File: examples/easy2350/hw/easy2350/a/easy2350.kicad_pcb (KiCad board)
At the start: 4 copper layers, 21 x 51 mm, 58 parts, among them J1 USB-C, J2 GPIO left, J3 GPIO right, J4 SWD, SW1 BOOTSEL, SW2 RESET, U1 RP2350A, U2 USBLC6-2SC6, U3 AP7361C-33FGE, U4 SN74LV1T125DBVR, U5 W25Q128JVSIQ, Y1 12MHz

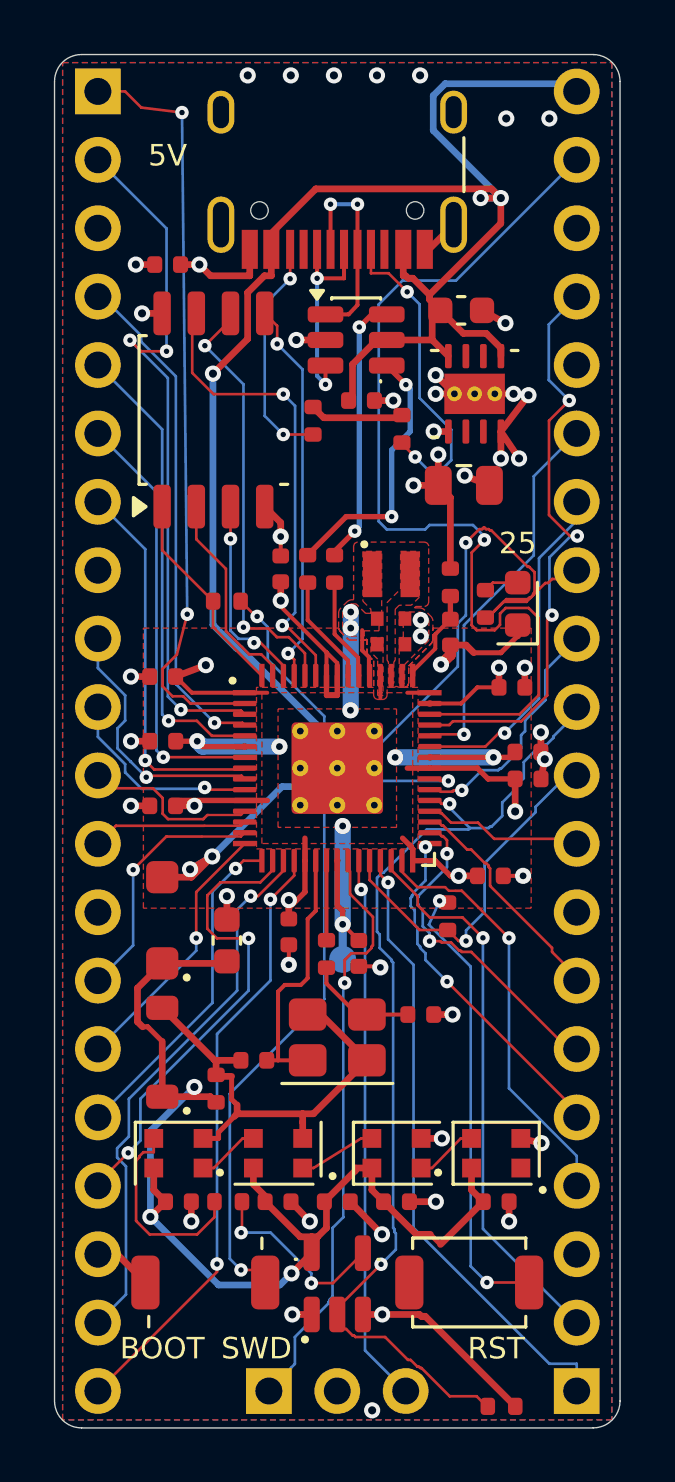
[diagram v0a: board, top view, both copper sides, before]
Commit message: easy2350: re-routed with ultraroute from a bare board, no locked copper
The user: easy2350 should not be locked like that; it should route
deterministically with ultraroute. Every locked track and via is gone (the
vendor regulator copy, the critical pre-routes, the pad vias, the band stubs
and VBUS twins: 232 items) and the router lays the whole board. Footprints are
locked only where Circuit Composer's floorplan spec fixes them (J1-J4, U1, C14,
C15, L1, TP3, SW1, SW2, D1, D3-D6); board.py no longer locks copper anywhere.
ultraroute pinned at 63679d9.

Seeds 0-3 each leave one connection open, VREG_LX U1-48 to L1-2 (the router
can't reach the QFN pin past C14/C15), now asked of ultraroute; DRC also has one
+1V1 via in a silk no-via area. Gates 7-10 are stale and the release is off
until they pass again; status.json, the gate files and decisions.md say so.
LESSONS.md and routing.md: no locked copper. Renders and viewer rebuilt.

Co-Authored-By: Claude Opus 5.5 <noreply@anthropic.com>
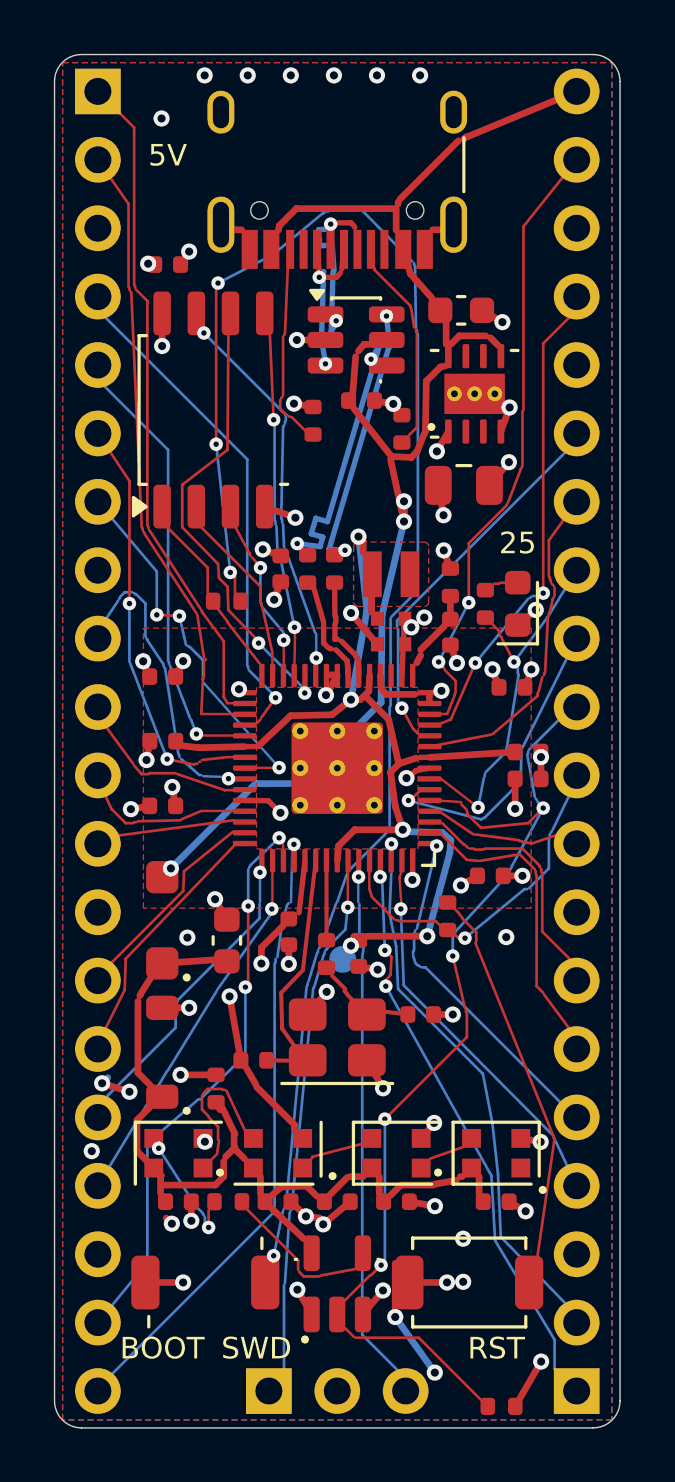
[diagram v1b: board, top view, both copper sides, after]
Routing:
- net Net-(R7-Pad2): track 28.9 -> 57.6 mm, vias 2 -> 4
- net VBUS: track 71.0 -> 47.3 mm, vias 5 -> 3
- net +3V3: track 43.0 -> 21.6 mm, vias 12 -> 23
- net GND: track 67.5 -> 47.5 mm, vias 43 -> 54
- net VLED: track 42.2 -> 24.8 mm, vias 3 -> 0
- net /GPIO29: track 35.9 -> 22.3 mm, vias 1 -> 2
- net /GPIO25: track 22.8 -> 13.1 mm
- net +1V1: track 26.4 -> 35.2 mm, vias 9 -> 5
- net /GPIO0: track 28.4 -> 23.1 mm, vias 2 -> 0
- net /GPIO28: track 22.0 -> 16.8 mm, vias 3 -> 2
- net /CC1: track 11.8 -> 6.78 mm, vias 2 -> 0
- net /GPIO1: track 26.6 -> 22.1 mm, vias 3 -> 0
- net /GPIO13: track 17.6 -> 13.5 mm, vias 2 -> 1
- net /QSPI_SD3: track 17.4 -> 13.4 mm
- net /LED_DIN: track 7.52 -> 4.03 mm, vias 0 -> 2
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- removed copper zone on F.Cu, net +1V1
- removed copper zone on F.Cu, net /VREG_LX

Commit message: easy2350: routed completely with ultraroute 770ef73, DRC 0 errors and 0 unconnected
The regulator corner and U1's pad ring were tracks keepouts left from the
locked-vendor-copper days; with the router laying that copper they blocked
L1's own pads (VREG_LX was open on every seed). Now named rule areas with
.kicad_dru rules that keep other nets out and let the corner's own in.
nets.csv length limits and XIN's no-via rule are in the dru, so KiCad and
autoroute.py's seed judge enforce them; the J2 labels are hard no-via areas
again; U1's pin-1 dot spot is reserved; the L2 cut-out covers the VREG_LX
pad hull before routing. Gates 7-10 still await review.

Co-Authored-By: Claude Opus 5.5 <noreply@anthropic.com>
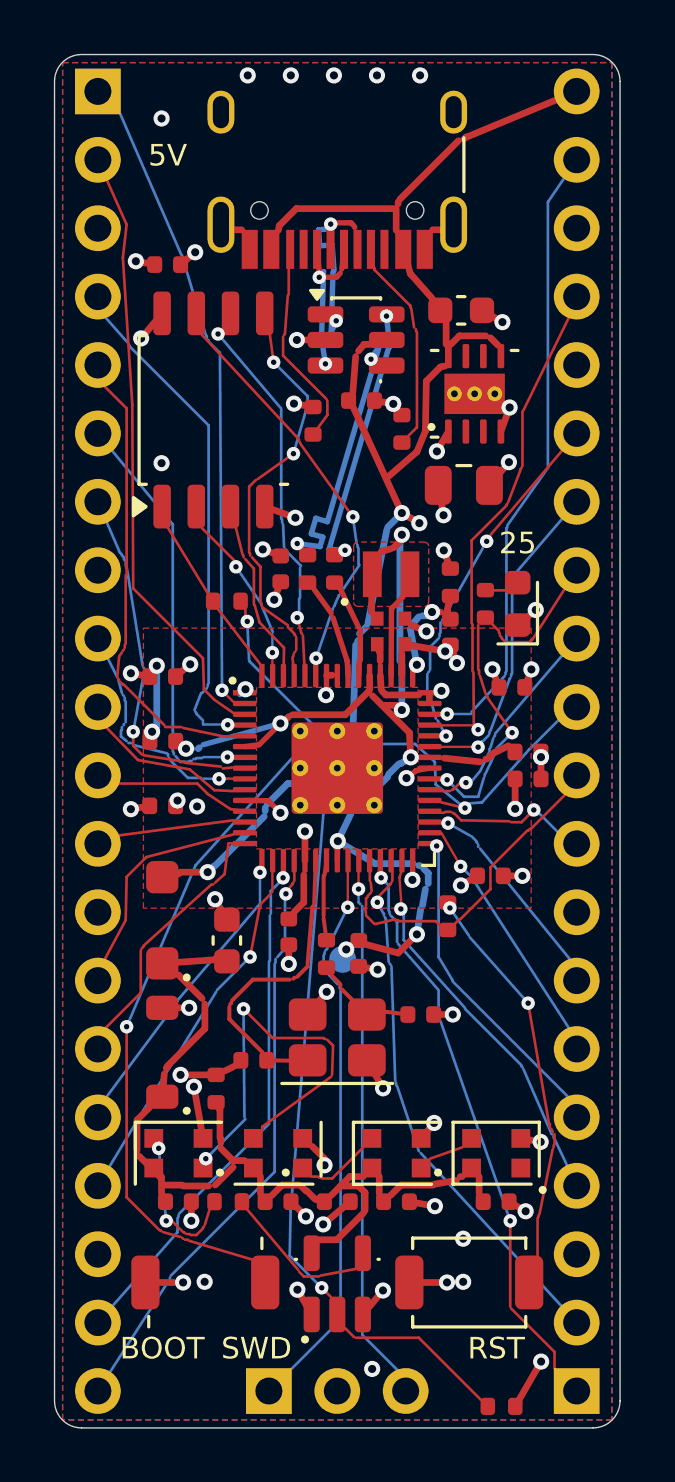
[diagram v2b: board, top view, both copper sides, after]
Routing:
- net Net-(R7-Pad2): track 57.6 -> 30.1 mm, vias 4 -> 2
- net /PIX12: track 4.99 -> 14.2 mm, vias 0 -> 2
- net +3V3: track 21.6 -> 17.4 mm, vias 23 -> 19
- net GND: track 47.5 -> 43.5 mm, vias 54 -> 53
- net /GPIO24: track 11.1 -> 7.50 mm
- net /GPIO23: track 34.9 -> 38.4 mm, vias 4 -> 2
- net /VREG_LX: track 0.00 -> 3.08 mm
- net /QSPI_SCLK: track 16.6 -> 13.5 mm
- net VLED: track 24.8 -> 27.4 mm
- net /QSPI_SD0: track 12.1 -> 14.1 mm
- net /GPIO14: track 21.0 -> 19.1 mm, vias 3 -> 1
- net /GPIO6: track 9.59 -> 7.75 mm
- net /XIN: track 8.17 -> 9.84 mm
- net /GPIO17: track 20.4 -> 18.9 mm
- net /GPIO20: track 10.1 -> 8.62 mm, vias 0 -> 1
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
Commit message: easy2350: RP2350 reference pours as zones, layout review fixes in progress
The independent layout review (2026-10-31) found the router-laid regulator
copper (1V1 as 0.2 mm wire, a 9 mm FB loop), PIX12 between the crystal's
pads, vias drilled in SMD pads and footprint silk over vias. The user chose
the reference pours as zones: board.py regzones brings Raspberry Pi's
1V1 ring, 3V3 band and regulator-corner pours across relative to U1,
unlocked, and the router joins them. New dru rules keep the crystal to its
own nets and via holes out of SMD pads (router support requested). The
silk stage trims footprint silk at router vias; stitch.py keeps off all
silk and silk_check tests footprint silk against vias. ultraroute pinned to
0b9016f (routes to length rules). Gates 7-10 still stale.

Co-Authored-By: Claude Opus 5.5 <noreply@anthropic.com>
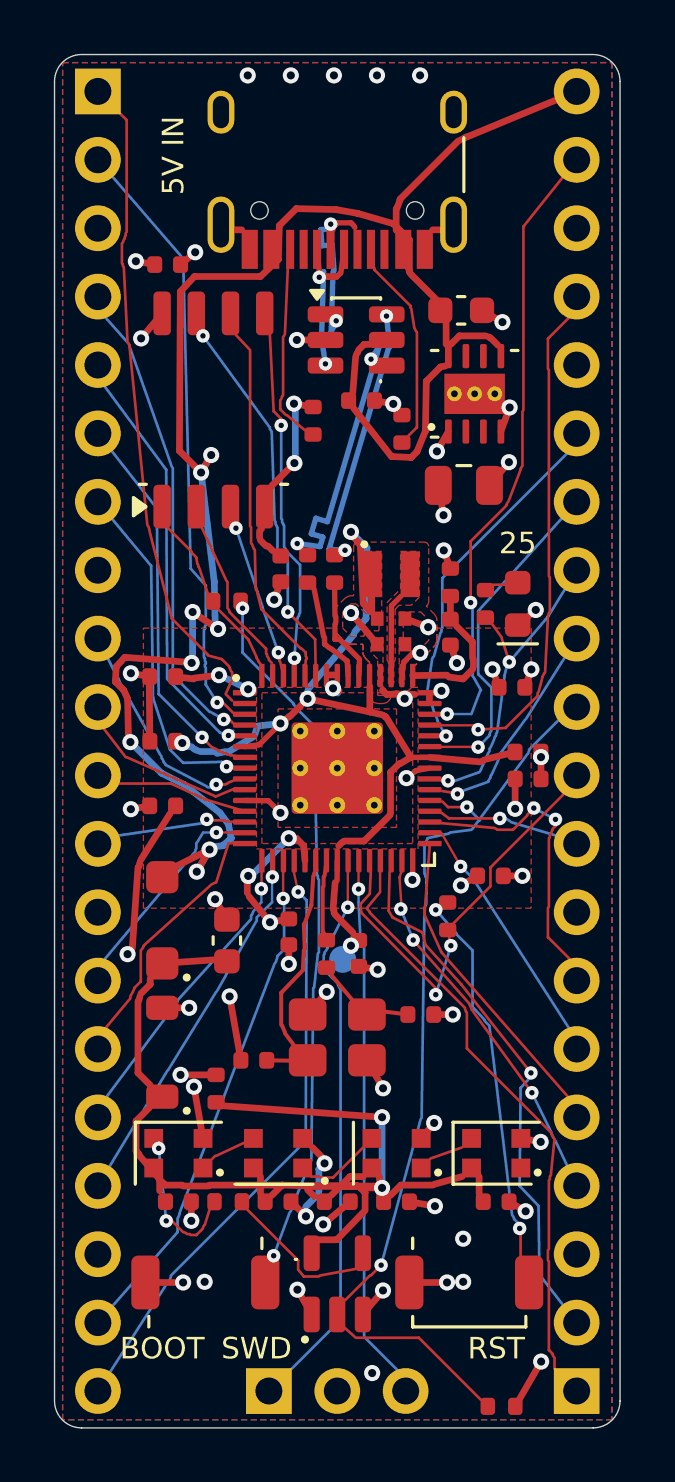
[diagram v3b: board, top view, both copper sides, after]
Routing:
- net VBUS: track 46.6 -> 67.4 mm, vias 3 -> 8
- net /PIX12: track 14.2 -> 1.68 mm, vias 2 -> 0
- net VLED: track 27.4 -> 39.5 mm, vias 0 -> 2
- net +3V3: track 17.4 -> 28.3 mm, vias 19 -> 22
- net /GPIO23: track 38.4 -> 32.1 mm
- net Net-(R7-Pad2): track 30.1 -> 25.0 mm
- net /RUN: track 10.7 -> 15.6 mm, vias 0 -> 2
- net GND: track 43.5 -> 47.8 mm, vias 53 -> 49
- net /GPIO21: track 6.81 -> 10.0 mm, vias 1 -> 2
- net /XIN: track 9.84 -> 7.55 mm
- net /GPIO25: track 12.9 -> 11.3 mm
- net /VREG_AVDD: track 3.37 -> 4.88 mm, vias 2 -> 0
- net /QSPI_SD0: track 14.1 -> 12.7 mm
- net +1V1: track 35.1 -> 33.7 mm, vias 8 -> 5
- net /GPIO16: track 20.0 -> 21.1 mm, vias 2 -> 0
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- added copper zone on F.Cu, net +1V1
- added copper zone on F.Cu, net /VREG_LX
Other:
- board text added: "5V IN"
- board text removed: "5V"

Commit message: easy2350: re-routed on ultraroute 0b0f336, no via holes in SMD pads; DRC 0/0
Co-Authored-By: Claude Opus 5.5 <noreply@anthropic.com>
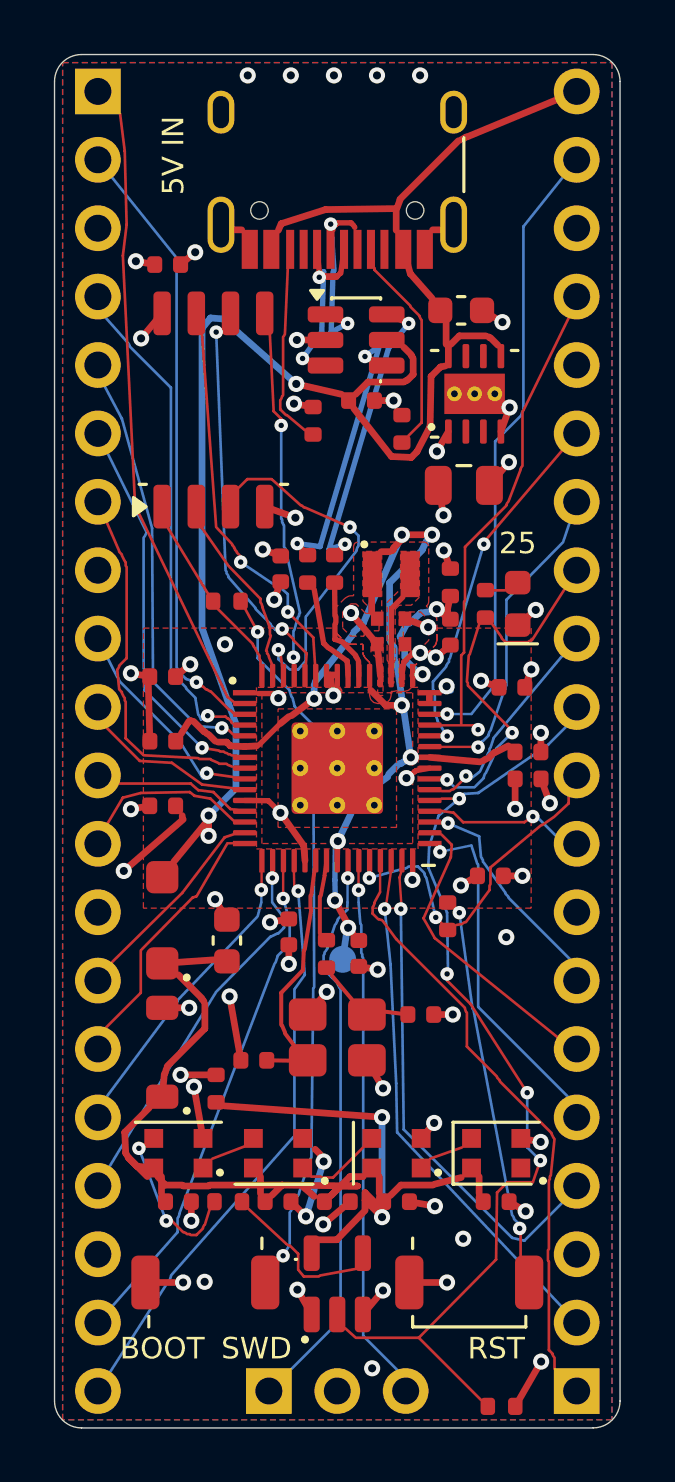
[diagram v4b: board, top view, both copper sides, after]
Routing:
- net VBUS: track 67.4 -> 57.1 mm, vias 8 -> 3
- net /QSPI_SD2: track 5.78 -> 12.9 mm
- net +3V3: track 28.3 -> 22.5 mm, vias 22 -> 20
- net /RUN: track 15.6 -> 10.8 mm
- net +1V1: track 33.7 -> 38.0 mm, vias 5 -> 8
- net /GPIO18: track 13.5 -> 17.7 mm, vias 3 -> 1
- net /GPIO23: track 32.1 -> 35.7 mm, vias 2 -> 4
- net /GPIO21: track 10.0 -> 7.12 mm, vias 2 -> 1
- net VLED: track 39.5 -> 42.4 mm
- net /GPIO9: track 4.34 -> 6.45 mm, vias 1 -> 0
- net /GPIO25: track 11.3 -> 13.1 mm
- net /GPIO20: track 8.73 -> 10.2 mm, vias 1 -> 0
- net GND: track 47.8 -> 46.5 mm, vias 49 -> 51
- net /USB_DM: track 9.95 -> 11.0 mm
- net /USB_DP_C: track 6.72 -> 7.69 mm
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
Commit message: easy2350: reference power tracks as zones; pad_joints.py catches thin pad entries
Second layout review (2026-11-01): the reference pours were in but no 1V1
zone touched a DVDD pin and FB ran 10 mm through two vias (A1); four pads
were joined only by a track end-cap's lens under the fab minimum (A2).
regzones now brings the reference's power tracks across as zones too
(top priority, islands kept), so pins 6, 23, 39 and 50 sit on reference
copper; the router must still join the spoke zones with vias (asked of
ultraroute). New skill check pad_joints.py finds thin pad joints DRC can't
see; routing.md lists it. Via rings now clear SMD pads (0.2 mm), VREG_AVDD
stays on top, and paste-only pads are out of the via rule.

Co-Authored-By: Claude Opus 5.5 <noreply@anthropic.com>
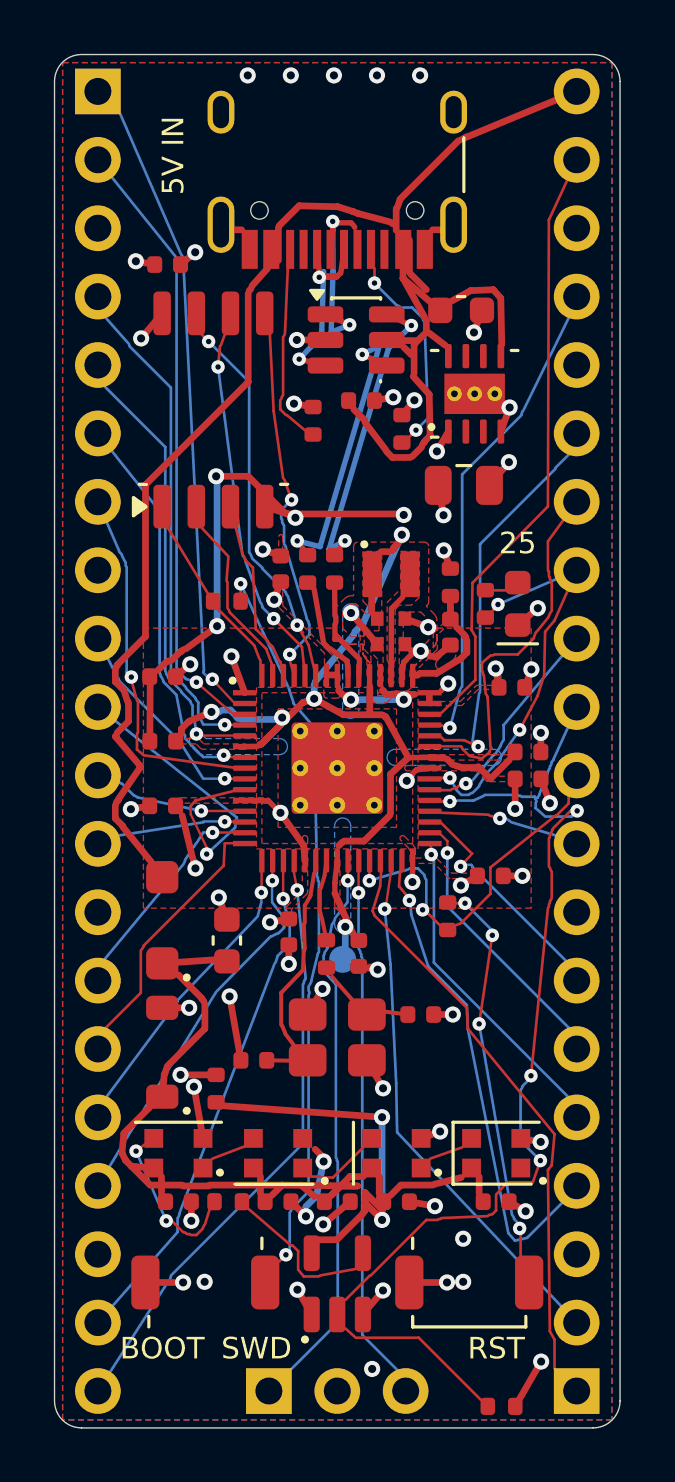
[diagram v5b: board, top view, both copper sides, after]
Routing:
- net GND: track 46.5 -> 62.3 mm, vias 51 -> 53
- net /QSPI_SD2: track 12.9 -> 5.85 mm, vias 2 -> 0
- net /GPIO7: track 5.47 -> 12.2 mm, vias 0 -> 1
- net +1V1: track 38.0 -> 34.1 mm, vias 8 -> 5
- net VBUS: track 57.1 -> 59.7 mm, vias 3 -> 0
- net /GPIO9: track 6.45 -> 4.29 mm, vias 0 -> 1
- net /GPIO23: track 35.7 -> 37.6 mm
- net Net-(R7-Pad2): track 24.8 -> 26.2 mm
- net +3V3: track 22.5 -> 23.9 mm
- net /GPIO26: track 11.5 -> 12.6 mm, vias 1 -> 0
- net /GPIO20: track 10.2 -> 9.12 mm, vias 0 -> 1
- net /GPIO25: track 13.1 -> 14.1 mm, vias 2 -> 3
- net /GPIO27: track 13.1 -> 14.0 mm, vias 2 -> 1
- net Net-(R8-Pad2): track 13.1 -> 14.0 mm, vias 2 -> 4
- net /GPIO28: track 17.6 -> 16.8 mm
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- added copper zone on B.Cu, net +1V1
- added copper zone on F.Cu, net /VREG_AVDD
